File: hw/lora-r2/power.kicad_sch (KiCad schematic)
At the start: 9 parts, among them J4 Conn_01x06, Q1 PMOS, U3 MCP1700-3302E_SOT23

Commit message: DRC passing
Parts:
- removed Q1: PMOS, symbol Simulation_SPICE:PMOS
- removed U3: MCP1700-3302E_SOT23, Package_TO_SOT_SMD:SOT-23, symbol Regulator_Linear:MCP1700-3302E_SOT23
- added Q1: FDN340P, Package_TO_SOT_SMD:SOT-23, symbol Transistor_FET:FDN340P
- added U3: MCP1700x-330xxTT, Package_TO_SOT_SMD:SOT-23, symbol Regulator_Linear:MCP1700x-330xxTT
- J4: footprint (none) -> Connector_PinHeader_2.54mm:PinHeader_1x06_P2.54mm_Vertical
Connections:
- net +3.3V: now also Q1.3 (D)
- net +3V3: now also U3.2 (VO)
- net 3V3_SWITCHED: now also Q1.2 (S)
- net GND: now also U3.1 (GND)
- net GPIO20: now also Q1.1 (G)
- net VCONV: now also U3.3 (VI)

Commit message: Working on PCB
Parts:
- removed Q1: FDN340P, Package_TO_SOT_SMD:SOT-23, symbol Transistor_FET:FDN340P
- added Q1: IRLML6401, Package_TO_SOT_SMD:SOT-23, symbol Transistor_FET:IRLML6401
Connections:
- net +3.3V: now also Q1.2 (S)
- net 3V3_SWITCHED: now also Q1.3 (D)
- net GPIO20: now also Q1.1 (G)
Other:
- note added: "High-side switch to turn on/off radio selectively."
- note added: "Source"
- note removed: "Need to check D/S polarity here!"
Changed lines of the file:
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@@
 		)
 	)
-	(text "Need to check D/S polarity here!"
-		(exclude_from_sim no)
-		(at 176.276 35.814 0)
+	(text "High-side switch to turn on/off radio selectively."
+		(exclude_from_sim no)
+		(at 170.18 30.48 0)
 		(effects
 			(font
 				(size 1.27 1.27)
-				(color 255 2 6 1)
+			)
+		)
+	)
+	(text "Source"
+		(exclude_from_sim no)
+		(at 163.576 48.26 0)
+		(effects
+			(font
+				(size 1.27 1.27)
 			)
 		)
@@
 		)
 	)
+	(text_box "~30K available on DigiKey.  SOT-23 footprint.\nRds(on) is 85mOhm at Vgs=-2.5V."
+		(exclude_from_sim no)
+		(at 173.99 50.165 0)
+		(size 48.895 6.35)
+		(margins 0.9525 0.9525 0.9525 0.9525)
+		(stroke
+			(width 0)
+			(type solid)
+		)
+		(fill
+			(type color)
+			(color 117 204 255 1)
+		)
+		(effects
+			(font
+				(size 1.27 1.27)
+			)
+			(justify left top)
+		)
+	)
 	(junction
 		(at 50.8 41.91)
@@
 	)
 	(symbol
+		(lib_id "Transistor_FET:IRLML6401")
+		(at 170.18 48.26 270)
+		(mirror x)
+		(unit 1)
+		(exclude_from_sim no)
+		(in_bom yes)
+		(on_board yes)
+		(dnp no)
+		(property "Reference" "Q1"
+			(at 170.18 39.37 90)
+			(effects
+				(font
+					(size 1.27 1.27)
+				)
+			)
+		)
+		(property "Value" "IRLML6401"
+			(at 170.18 41.91 90)
+			(effects
+				(font
+					(size 1.27 1.27)
+				)
+			)
+		)
+		(property "Footprint" "Package_TO_SOT_SMD:SOT-23"
+			(at 168.275 43.18 0)
+			(effects
+				(font
+					(size 1.27 1.27)
+					(italic yes)
+				)
+				(justify left)
+				(hide yes)
+			)
+		)
+		(property "Datasheet" "https://www.infineon.com/dgdl/irlml6401pbf.pdf?fileId=5546d462533600a401535668b96d2634"
+			(at 153.924 62.738 90)
+			(effects
+				(font
+					(size 1.27 1.27)
+				)
+				(justify left)
+			)
+		)
+		(property "Description" "-4.3A Id, -12V Vds, 50mOhm Rds, P-Channel HEXFET Power MOSFET, SOT-23"
+			(at 170.18 48.26 0)
+			(effects
+				(font
+					(size 1.27 1.27)
+				)
+				(hide yes)
+			)
+		)
+		(pin "2"
+		)
+		(pin "1"
+		)
+		(pin "3"
+		)
+		(instances
+			(project ""
+				(path "/7c949457-b1cf-485c-aaec-4142bb885473/1480c633-6832-4a00-ad6f-0d91d4f73ed1"
+					(reference "Q1")
+					(unit 1)
+				)
+			)
+		)
+	)
+	(symbol
 		(lib_id "power:PWR_FLAG")
 		(at 148.59 45.72 0)
@@
 					(unit 1)
 				)
-			)
-		)
-	)
-	(symbol
-		(lib_id "Transistor_FET:FDN340P")
-		(at 170.18 48.26 90)
-		(unit 1)
-		(exclude_from_sim no)
-		(in_bom yes)
-		(on_board yes)
-		(dnp no)
-		(fields_autoplaced yes)
-		(property "Reference" "Q1"
-			(at 170.18 39.37 90)
-			(effects
-				(font
-					(size 1.27 1.27)
-				)
-			)
-		)
-		(property "Value" "FDN340P"
-			(at 170.18 41.91 90)
-			(effects
-				(font
-					(size 1.27 1.27)
-				)
-			)
-		)
-		(property "Footprint" "Package_TO_SOT_SMD:SOT-23"
-			(at 172.085 43.18 0)
-			(effects
-				(font
-					(size 1.27 1.27)
-					(italic yes)
-				)
-				(justify left)
-				(hide yes)
-			)
-		)
-		(property "Datasheet" "https://www.onsemi.com/pub/Collateral/FDN340P-D.PDF"
-			(at 173.99 43.18 0)
-			(effects
-				(font
-					(size 1.27 1.27)
-				)
-				(justify left)
-				(hide yes)
-			)
-		)
-		(property "Description" "-2A Id, -20V Vds, P-Channel MOSFET, 70mOhm Ron, SOT-23"
-			(at 170.18 48.26 0)
-			(effects
-				(font
-					(size 1.27 1.27)
-				)
-				(hide yes)
-			)
-		)
-		(pin "2"
-		)
-		(pin "1"
-		)
-		(pin "3"
-		)
-		(instances
-			(project ""
-				(path "/7c949457-b1cf-485c-aaec-4142bb885473/1480c633-6832-4a00-ad6f-0d91d4f73ed1"
-					(reference "Q1")
-					(unit 1)
-				)

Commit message: Making progress on layout
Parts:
- removed C5: 10u, Capacitor_SMD:CP_Elec_4x5.4, symbol Device:C_Polarized_Small
- removed J4: Conn_01x06, Connector_PinHeader_2.54mm:PinHeader_1x06_P2.54mm_Vertical, symbol Connector_Generic:Conn_01x06
- added C1: 10u, Capacitor_SMD:C_0805_2012Metric_Pad1.18x1.45mm_HandSolder, symbol Device:C_Small
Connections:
- net +3V3 is gone; now on net +3.3V: U3.2 (VO)
- net VCONV is gone; now on net VCON: C2.1, U3.3 (VI)
- net +3.3V: now also C1.1
- net GND: now also C1.2
- net GPIO20 renamed GPIO15
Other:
- note added: "Low ESR tantalum"
- note removed: "Panel voltage can be routed back to converter input on pin 2."

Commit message: Generated first Gerbers
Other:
- company: (none) -> Bruce MacKinnon
- title: (none) -> KC1FSZ LoRa Controller Board
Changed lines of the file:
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@@
 	(generator "eeschema")
 	(generator_version "9.0")
-	(paper "A4")
+	(paper "USLetter")
+	(title_block
+		(title "KC1FSZ LoRa Controller Board")
+		(date "2025-05-08")
+		(rev "1")
+		(company "Bruce MacKinnon")
+		(comment 1 "Copyright (C) 2025, Bruce MacKinnon")
+		(comment 2 "NOT FOR COMMERCIAL USE")
+	)
 	(text "High-side switch to turn on/off radio selectively."
 		(exclude_from_sim no)

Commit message: SENT TO FAB (2025-05-08 13:04)
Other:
- note added: "NOTE: Make sure this cap can handle +12V!"
- note added: "Voltage dividers to allow higher voltages to be monitored via 3.3V ADC."
- note removed: "Voltage Dividers"
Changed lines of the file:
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@@
 		(comment 2 "NOT FOR COMMERCIAL USE")
+	)
+	(text "NOTE: Make sure this \ncap can handle +12V!"
+		(exclude_from_sim no)
+		(at 54.61 66.04 0)
+		(effects
+			(font
+				(size 1.27 1.27)
+			)
+		)
 	)
 	(text "High-side switch to turn on/off radio selectively."
@@
 		)
 	)
-	(text "Voltage Dividers "
-		(exclude_from_sim no)
-		(at 24.13 92.71 0)
+	(text "Voltage dividers to allow higher voltages\nto be monitored via 3.3V ADC."
+		(exclude_from_sim no)
+		(at 73.406 89.662 0)
 		(effects
 			(font
@@
 				)
 				(justify left)
-			)
-		)
+				(hide yes)
+			)
+		)

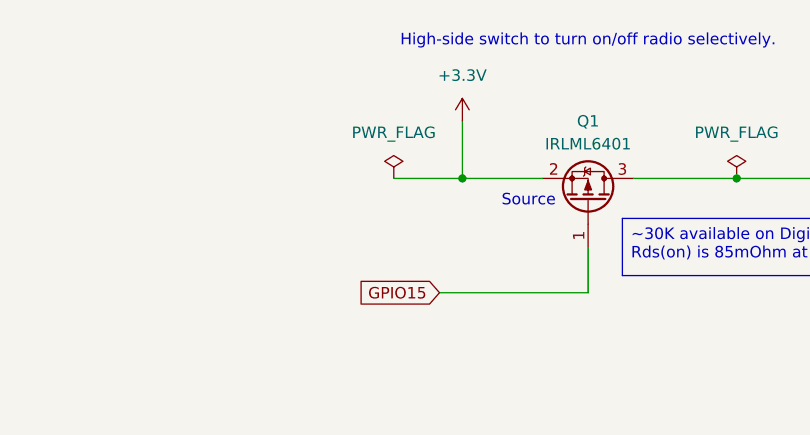
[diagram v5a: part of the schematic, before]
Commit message: Revision (before fab) - can power radio from USB now
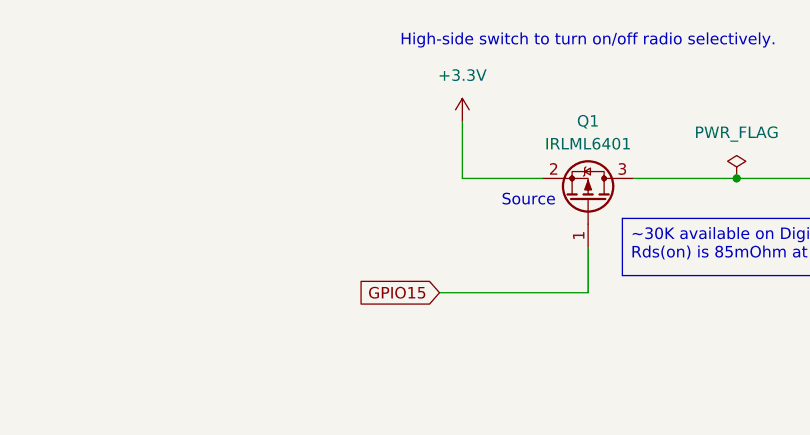
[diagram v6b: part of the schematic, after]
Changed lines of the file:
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@@
 	(title_block
 		(title "KC1FSZ LoRa Controller Board")
-		(date "2025-05-08")
+		(date "2025-05-11")
 		(rev "1")
 		(company "Bruce MacKinnon")
@@
 	)
 	(junction
-		(at 156.21 45.72)
-		(diameter 0)
-		(color 0 0 0 0)
-	)
-	(junction
 		(at 82.55 41.91)
 		(diameter 0)
@@
 		(pts
 			(xy 54.61 41.91) (xy 59.69 41.91)
-		)
-		(stroke
-			(width 0)
-			(type default)
-		)
-	)
-	(wire
-		(pts
-			(xy 148.59 45.72) (xy 156.21 45.72)
 		)
 		(stroke
@@
 					(unit 1)
 				)
-			)
-		)
-	)
-	(symbol
-		(lib_id "power:PWR_FLAG")
-		(at 148.59 45.72 0)
-		(unit 1)
-		(exclude_from_sim no)
-		(in_bom yes)
-		(on_board yes)
-		(dnp no)
-		(fields_autoplaced yes)
-		(property "Reference" "#FLG04"
-			(at 148.59 43.815 0)
-			(effects
-				(font
-					(size 1.27 1.27)
-				)
-				(hide yes)
-			)
-		)
-		(property "Value" "PWR_FLAG"
-			(at 148.59 40.64 0)
-			(effects
-				(font
-					(size 1.27 1.27)
-				)
-			)
-		)
-		(property "Footprint" ""
-			(at 148.59 45.72 0)
-			(effects
-				(font
-					(size 1.27 1.27)
-				)
-				(hide yes)
-			)
-		)
-		(property "Datasheet" "~"
-			(at 148.59 45.72 0)
-			(effects
-				(font
-					(size 1.27 1.27)
-				)
-				(hide yes)
-			)
-		)
-		(property "Description" "Special symbol for telling ERC where power comes from"
-			(at 148.59 45.72 0)
-			(effects
-				(font
-					(size 1.27 1.27)
-				)
-				(hide yes)
-			)
-		)
-		(pin "1"
-		)
-		(instances
-			(project ""
-				(path "/7c949457-b1cf-485c-aaec-4142bb885473/1480c633-6832-4a00-ad6f-0d91d4f73ed1"
-					(reference "#FLG04")
-					(unit 1)
-				)
